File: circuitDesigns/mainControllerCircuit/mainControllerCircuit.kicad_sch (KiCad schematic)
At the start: 72 parts, among them J1 USB_A, J13 Moon, J14 LS1-3, J15 SS1-4, J16 SS5-8, J17 SS9-12, J18 LightSensor, J19 OutGND, J2 USB_A, J3 USB_A, J4 Conn_01x15_Pin, J5 Conn_01x15_Pin, J6 Out3V3, J7 OutputVCC, Q1 AO3400A, Q10 AO3400A, Q11 AO3400A, Q12 AO3400A, Q13 AO3400A, Q14 AO3400A, Q15 AO3400A, Q16 AO3400A, Q2 AO3400A, Q3 AO3400A, Q4 AO3400A, Q5 AO3400A, Q6 AO3400A, Q7 AO3400A, Q8 AO3400A, Q9 AO3400A

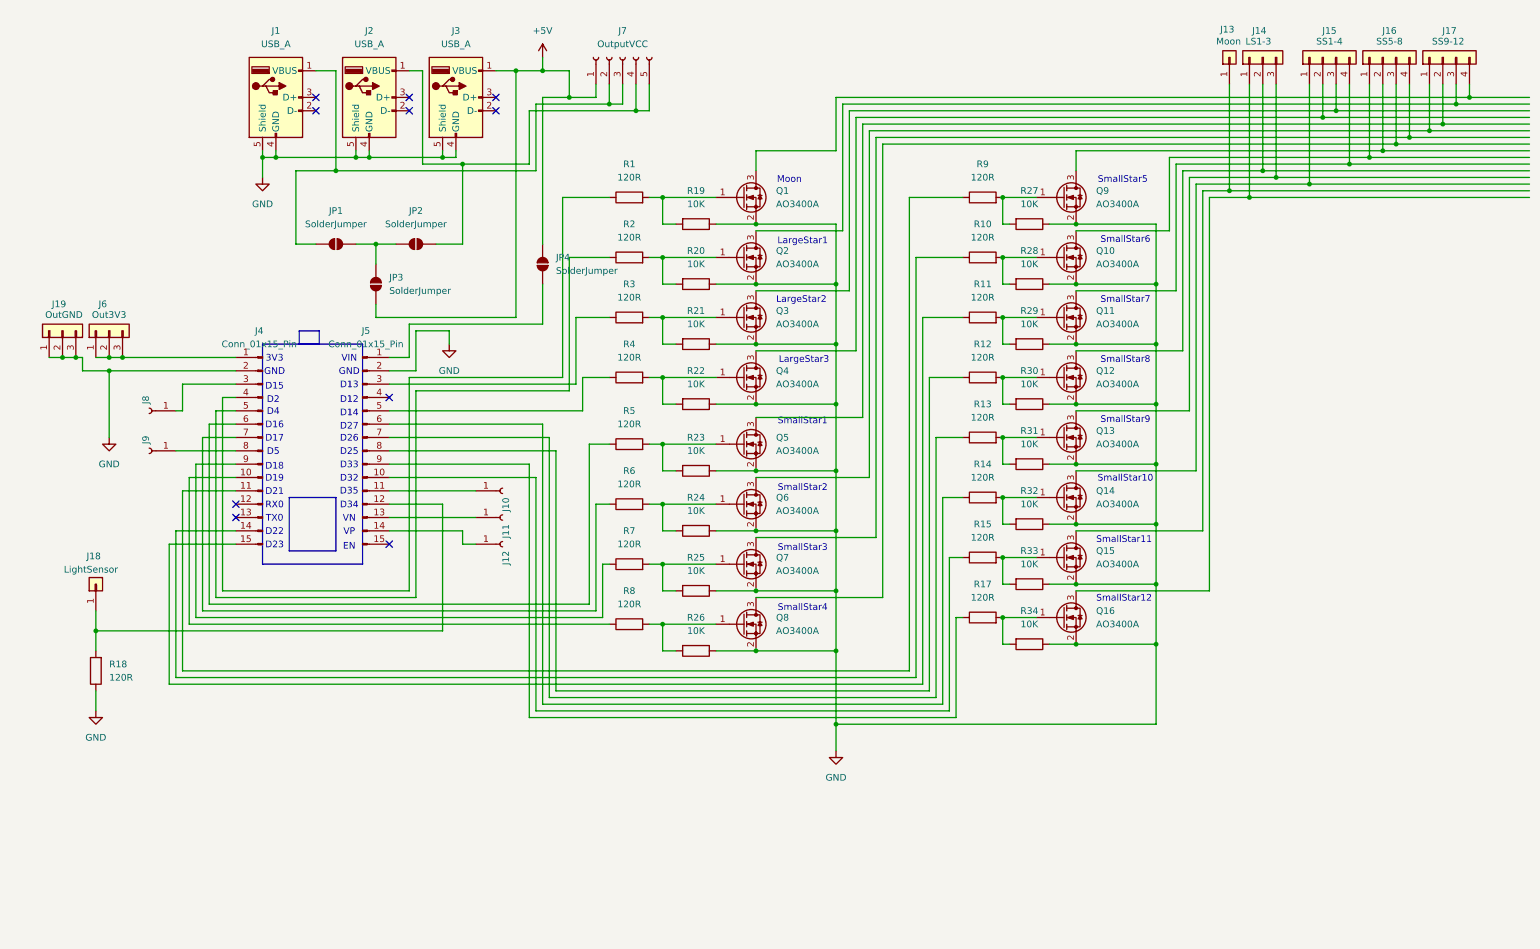
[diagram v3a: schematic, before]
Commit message: Adds LED indicators to the main controller board
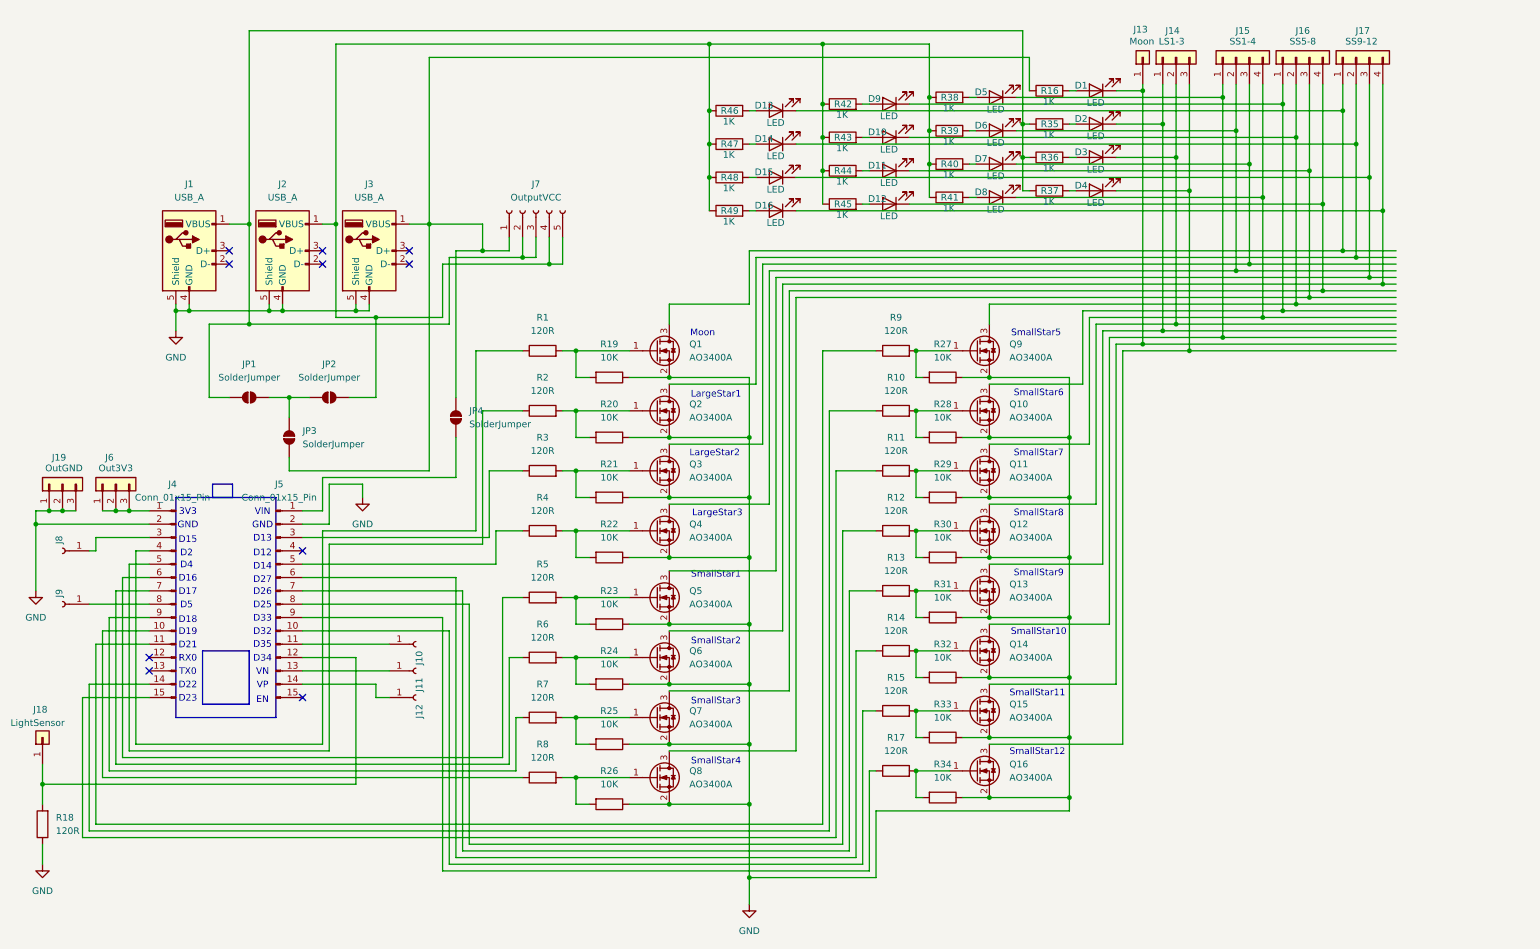
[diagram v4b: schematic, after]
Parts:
- added D1, D10, D11, D12, D13, D14, D15, D16, D2, D3, D4, D5, D6, D7, D8, D9: LED, LED_THT:LED_D3.0mm, symbol Device:LED
- added R16, R35, R36, R37, R38, R39, R40, R41, R42, R43, R44, R45, R46, R47, R48, R49: 1K, Resistor_THT:R_Axial_DIN0207_L6.3mm_D2.5mm_P7.62mm_Horizontal, symbol Device:R
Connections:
- net at J15.4 (Pin_4), Q11.3 (D): now also D8.1 (K)
- net at Q13.3 (D): now also J14.1 (Pin_1), D2.1 (K); no longer J14.3 (Pin_3)
- net at J16.4 (Pin_4), Q7.3 (D): now also D12.1 (K)
- net at J15.2 (Pin_2), Q4.3 (D): now also D6.1 (K)
- net at Q1.3 (D): now also J17.1 (Pin_1), D13.1 (K); no longer J17.4 (Pin_4)
- net at Q6.3 (D): now also J17.4 (Pin_4), D16.1 (K); no longer J17.1 (Pin_1)
- net at J17.2 (Pin_2): now also Q2.3 (D), D14.1 (K); no longer Q5.3 (D)
- net at J17.3 (Pin_3): now also Q5.3 (D), D15.1 (K); no longer Q2.3 (D)
- net at J16.3 (Pin_3), Q8.3 (D): now also D11.1 (K)
- net at J14.2 (Pin_2), Q12.3 (D): now also D3.1 (K)
- net at J15.1 (Pin_1), Q14.3 (D): now also D5.1 (K)
- net at J2.1 (VBUS), J7.4 (Pin_4), J7.5 (Pin_5)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: now also R38.1, R39.1, R40.1, R41.1, R42.1, R43.1, R44.1, R45.1, R46.1, R47.1, R48.1, R49.1
- net at J16.1 (Pin_1), Q10.3 (D): now also D9.1 (K)
- net at J1.1 (VBUS), J7.2 (Pin_2), J7.3 (Pin_3)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: now also R35.1, R36.1, R37.1
- net at J13.1 (Pin_1), Q15.3 (D): now also D1.1 (K)
- net at J15.3 (Pin_3), Q3.3 (D): now also D7.1 (K)
- net at J16.2 (Pin_2), Q9.3 (D): now also D10.1 (K)
- net at Q16.3 (D): now also J14.3 (Pin_3), D4.1 (K); no longer J14.1 (Pin_1)
- net +5V: no longer names the net of J3.1 (VBUS), J7.1 (Pin_1), JP3.1 (A), JP4.2 (B)
- net +5V: now also R16.1
- new net: D10.2 (A), R43.2
- new net: D9.2 (A), R42.2
- new net: D14.2 (A), R47.2
- new net: D13.2 (A), R46.2
- new net: D8.2 (A), R41.2
- new net: D15.2 (A), R48.2
- new net: D3.2 (A), R36.2
- new net: D11.2 (A), R44.2
- new net: D6.2 (A), R39.2
- new net: D4.2 (A), R37.2
- new net: D1.2 (A), R16.2
- new net: D12.2 (A), R45.2
- new net: D5.2 (A), R38.2
- new net: D7.2 (A), R40.2
- new net: D16.2 (A), R49.2
- new net: D2.2 (A), R35.2
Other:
- moved on the sheet: J1, J10, J11, J12, J13, J14, J15, J16, J17, J18, J19, J2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
